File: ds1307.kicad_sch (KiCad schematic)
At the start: 7 parts, among them U8 DS1307+, Y3 Crystal

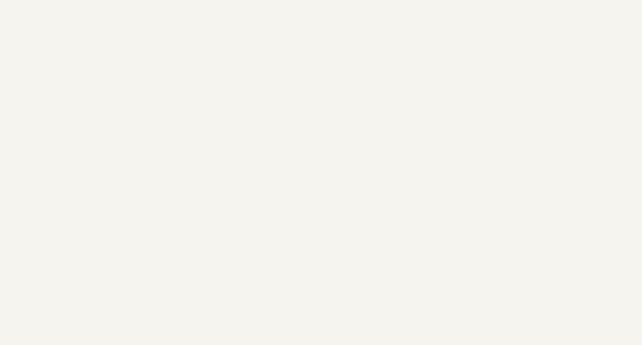
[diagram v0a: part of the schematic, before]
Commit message: Added schematic descriptions
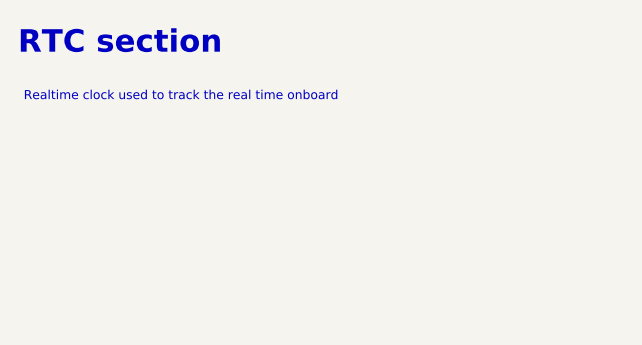
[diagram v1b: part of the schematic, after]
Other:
- note added: "RTC section"
- note added: "Realtime clock used to track the real time onboard"
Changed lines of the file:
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@@
   (title_block
     (title "Iron Warriors v2.0 ")
-    (date "2023-07-16")
+    (date "2023-08-01")
     (rev "1.1")
   )
@@
     (stroke (width 0) (type default) (color 0 0 0 0))
   )
+  (text "Realtime clock used to track the real time onboard"
+    (at 18.415 26.67 0)
+    (effects (font (size 1 1)) (justify left bottom))
+  )
+  (text "RTC section" (at 17.78 21.59 0)
+    (effects (font (size 2.5 2.5) (thickness 0.254) bold) (justify left bottom))
+  )
   (global_label "ds1307_sda" (shape input) (at 113.665 86.36 180) (fields_autoplaced)

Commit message: Added 12V regulator for injector
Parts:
- BT1: footprint (none) -> Battery:BatteryHolder_Keystone_3034_1x20mm
